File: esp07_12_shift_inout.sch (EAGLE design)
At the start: 47 parts, among them IC1 74HCT595D, IC2 74HCT595D, IC3 74HC165D, IC4 74HC165D

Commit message: Another approximation
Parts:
- JP11, JP12: value M02PTH3 -> (none); device SparkFun-Connectors:M02PTH3 -> SparkFun-Connectors:M02PTH
- JP7: value M02PTH3 -> (none)
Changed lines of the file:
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@@
 <part name="P+15" library="supply1" deviceset="VCC" device=""/>
 <part name="GND18" library="supply1" deviceset="GND" device=""/>
-<part name="JP11" library="SparkFun-Connectors" deviceset="M02" device="PTH3"/>
-<part name="JP12" library="SparkFun-Connectors" deviceset="M02" device="PTH3"/>
+<part name="JP11" library="SparkFun-Connectors" deviceset="M02" device="PTH"/>
+<part name="JP12" library="SparkFun-Connectors" deviceset="M02" device="PTH"/>
 <part name="GND19" library="supply1" deviceset="GND" device=""/>
 <part name="GND20" library="supply1" deviceset="GND" device=""/>

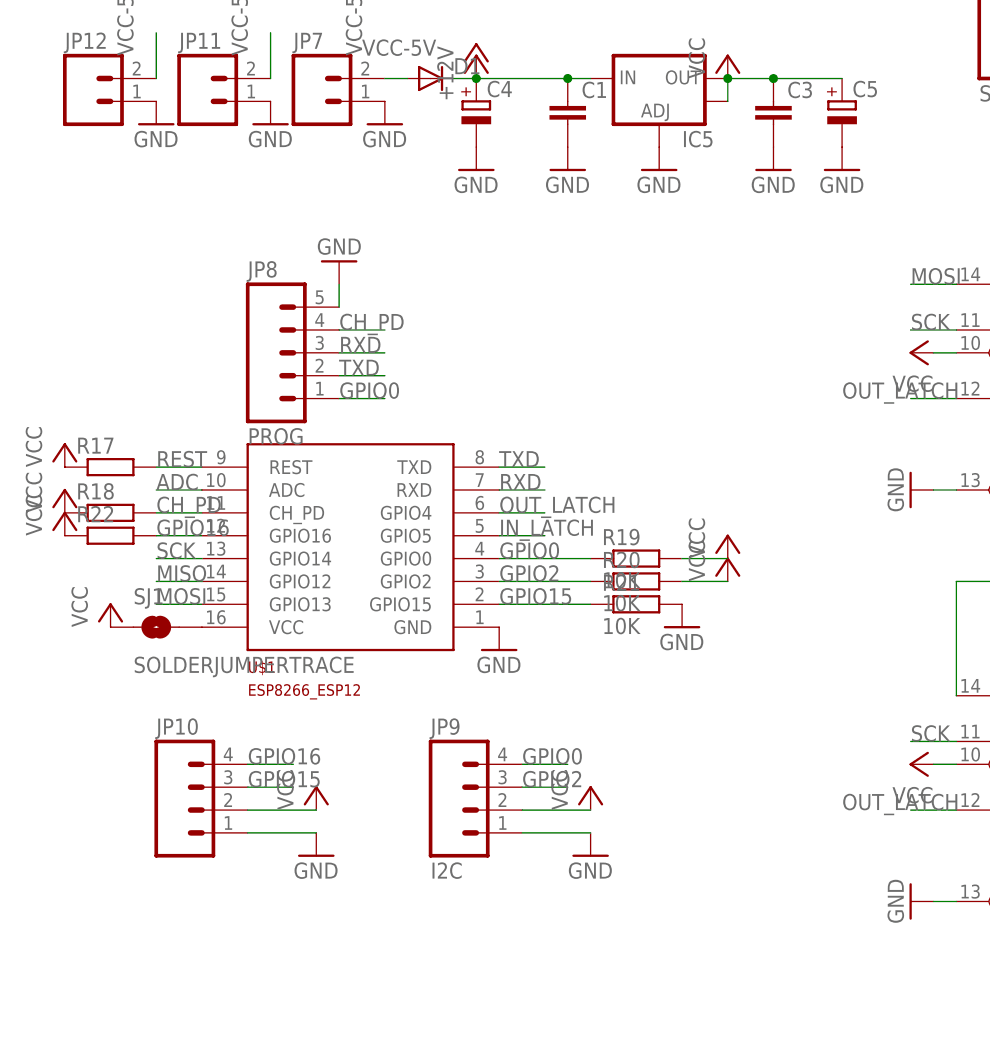
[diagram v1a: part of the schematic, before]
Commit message: * Change ESP module to ESP-12E footprint. Change ESP resistors to 0603. Change *_LATCH pins to 15,16
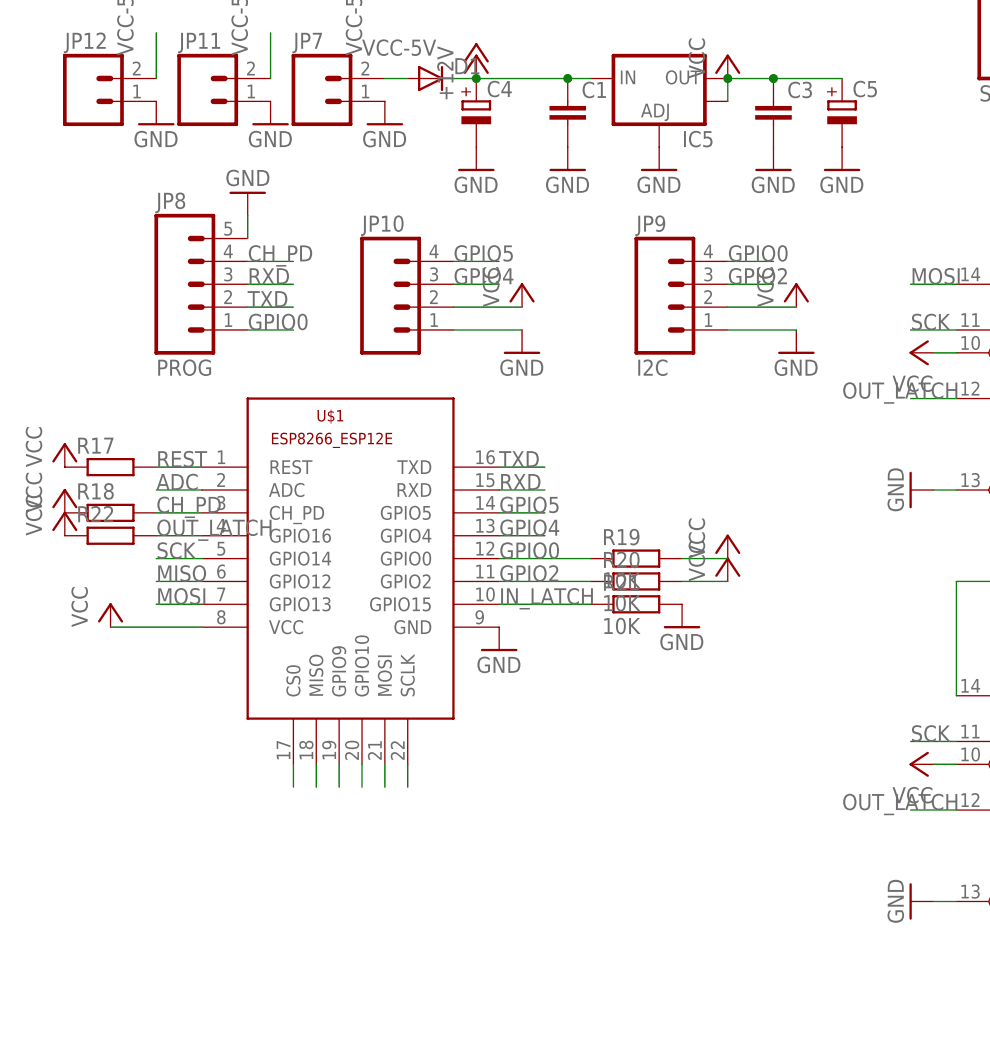
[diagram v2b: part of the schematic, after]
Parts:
- removed SJ1: SOLDERJUMPERTRACE, SparkFun-Retired:SOLDERJUMPERTRACE
- R17, R18, R19, R20, R21, R22: device rcl:R-EU_M0805 -> rcl:R-EU_R0603
- U$1: value ESP8266_ESP-12 -> (none); device esp8266_esp12:ESP8266_ESP-12 -> ESP8266-ESP12E:ESP8266-12EESP8266-ESP12E
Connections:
- removed net GPIO15: JP10.3, R21.1, U$1.GPIO15
- removed net GPIO16: JP10.4, R22.2, U$1.GPIO16
- removed net N$36: SJ1.2, U$1.VCC
- new net GPIO4: JP10.3, U$1.GPIO4
- new net GPIO5: JP10.4, U$1.GPIO5
- new net N$35: U$1.CS0
- new net N$37: U$1.MISO
- new net N$38: U$1.GPIO9
- new net N$39: U$1.GPIO10
- new net N$40: U$1.MOSI
- new net N$41: U$1.SCLK
- net IN_LATCH: now also R21.1, U$1.GPIO15; no longer U$1.GPIO5
- net OUT_LATCH: now also R22.2, U$1.GPIO16; no longer U$1.GPIO4
- net VCC: now also U$1.VCC; no longer SJ1.1
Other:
- moved on the sheet: JP10, JP8, JP9

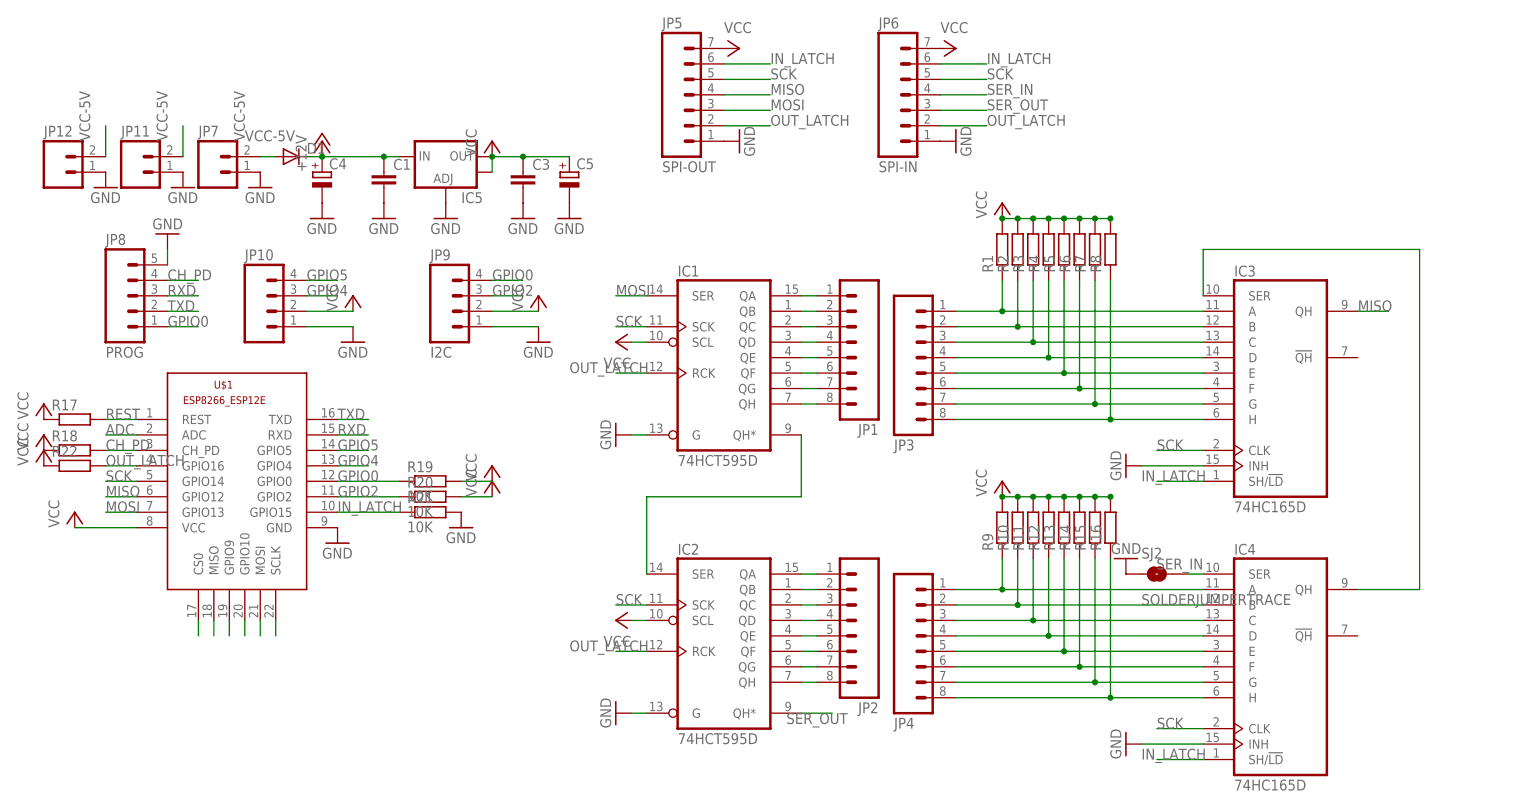
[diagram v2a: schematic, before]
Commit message: * Change OUT connectors to 2x10 and add GND / VCC pins to them
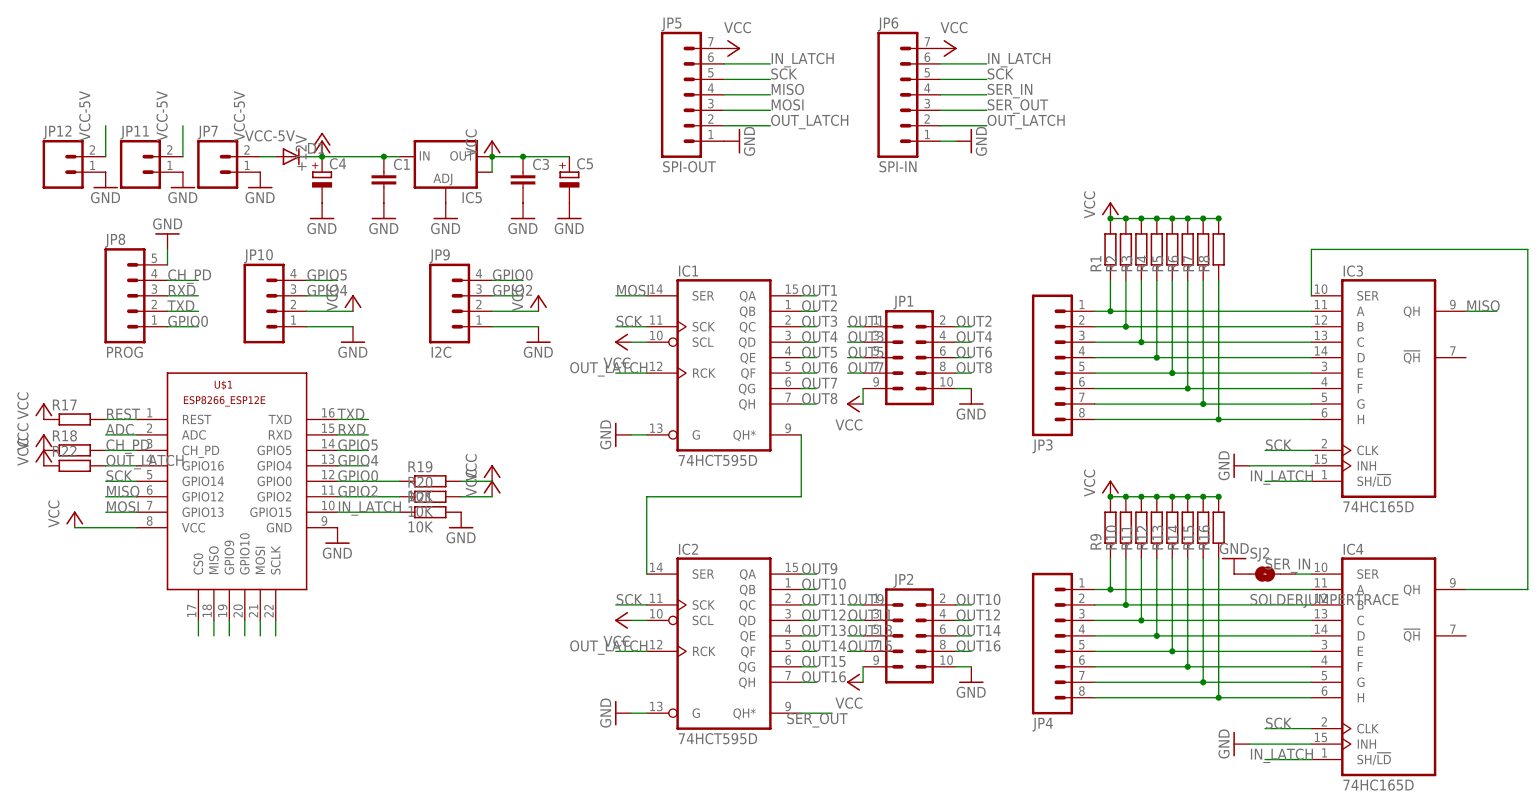
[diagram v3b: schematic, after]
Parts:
- JP1, JP2: device SparkFun-Connectors:M08SILK_FEMALE_PTH -> SparkFun-Connectors:M05X2PTH
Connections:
- net N$10 renamed OUT8
- net N$11 renamed OUT9
- net N$12 renamed OUT10
- net N$13 renamed OUT11
- net N$14 renamed OUT12
- net N$15 renamed OUT13
- net N$16 renamed OUT14
- net N$17 renamed OUT15
- net N$18 renamed OUT16
- net N$3 renamed OUT1
- net N$4 renamed OUT2
- net N$5 renamed OUT3
- net N$6 renamed OUT4
- net N$7 renamed OUT5
- net N$8 renamed OUT6
- net N$9 renamed OUT7
- net GND: now also JP1.10, JP2.10
- net VCC: now also JP1.9, JP2.9
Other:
- moved on the sheet: IC3, IC4, JP3, JP4, R1, R10, R11, R12, R13, R14, R15, R16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

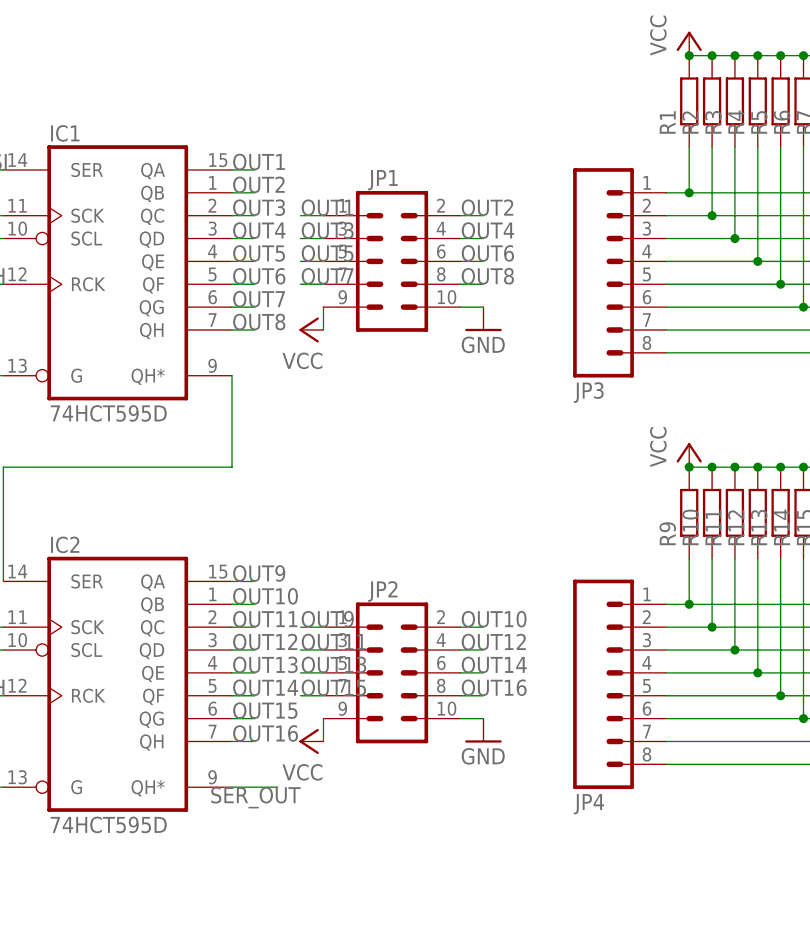
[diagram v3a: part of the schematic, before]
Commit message: * Change OUT pins configuration to pin 1 - GND, pin 10 - VCC
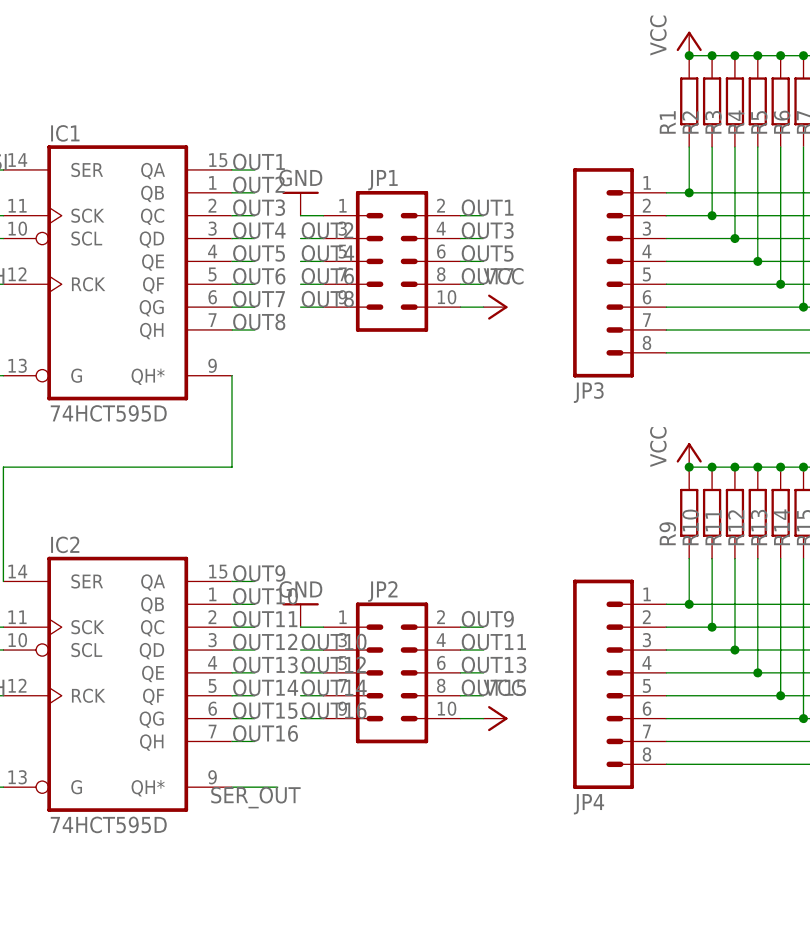
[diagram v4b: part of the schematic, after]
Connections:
- net GND: now also JP1.1, JP2.1; no longer JP1.10, JP2.10
- net OUT1: now also JP1.2; no longer JP1.1
- net OUT10: now also JP2.3; no longer JP2.2
- net OUT11: now also JP2.4; no longer JP2.3
- net OUT12: now also JP2.5; no longer JP2.4
- net OUT13: now also JP2.6; no longer JP2.5
- net OUT14: now also JP2.7; no longer JP2.6
- net OUT15: now also JP2.8; no longer JP2.7
- net OUT16: now also JP2.9; no longer JP2.8
- net OUT2: now also JP1.3; no longer JP1.2
- net OUT3: now also JP1.4; no longer JP1.3
- net OUT4: now also JP1.5; no longer JP1.4
- net OUT5: now also JP1.6; no longer JP1.5
- net OUT6: now also JP1.7; no longer JP1.6
- net OUT7: now also JP1.8; no longer JP1.7
- net OUT8: now also JP1.9; no longer JP1.8
- net OUT9: now also JP2.2; no longer JP2.1
- net VCC: now also JP1.10, JP2.10; no longer JP1.9, JP2.9

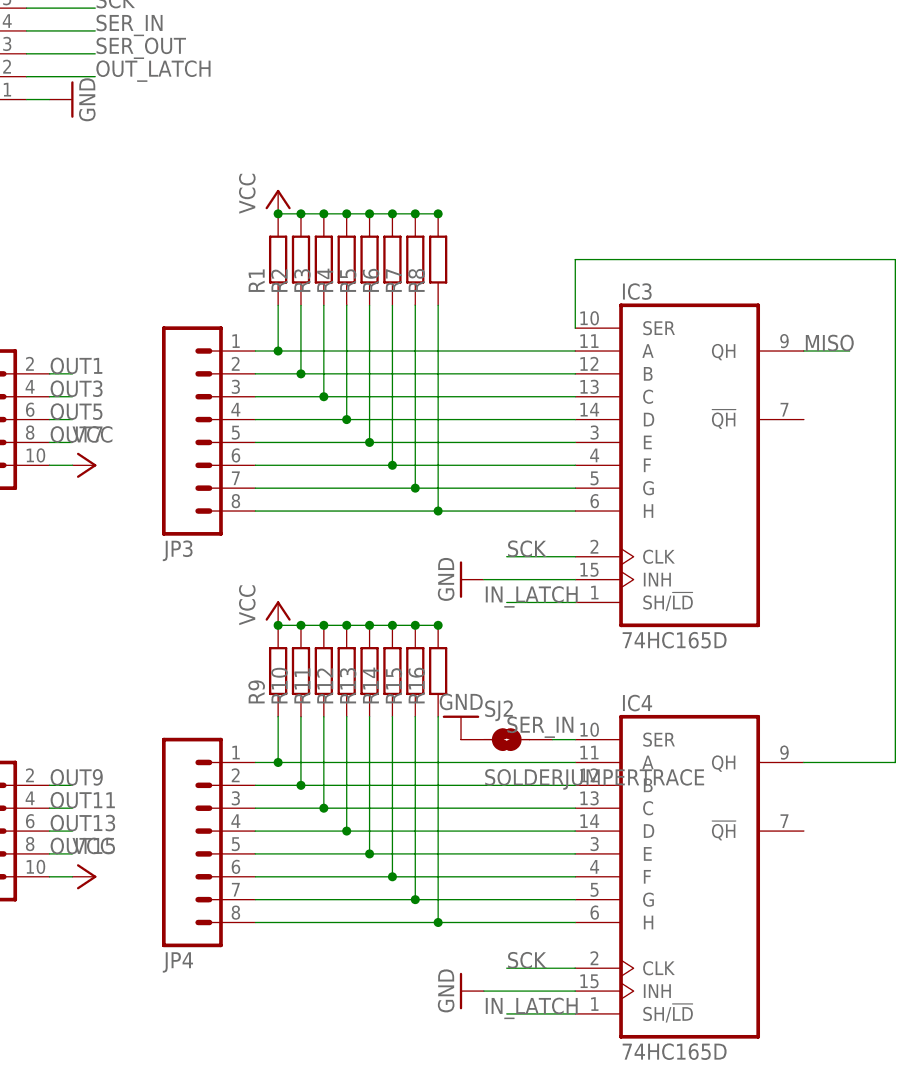
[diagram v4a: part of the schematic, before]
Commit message: * Finish new version of PCB.
* Change ESP module to ESP-12E with additional (but useless) pins
* Change OUT_ IN_ latch to 15,16
* Change OUT_ IN_ connection to 2x5 header
* Remove pull-up resistors on IN_ part in favour to implement them in add-on opto-isolated IN PCB
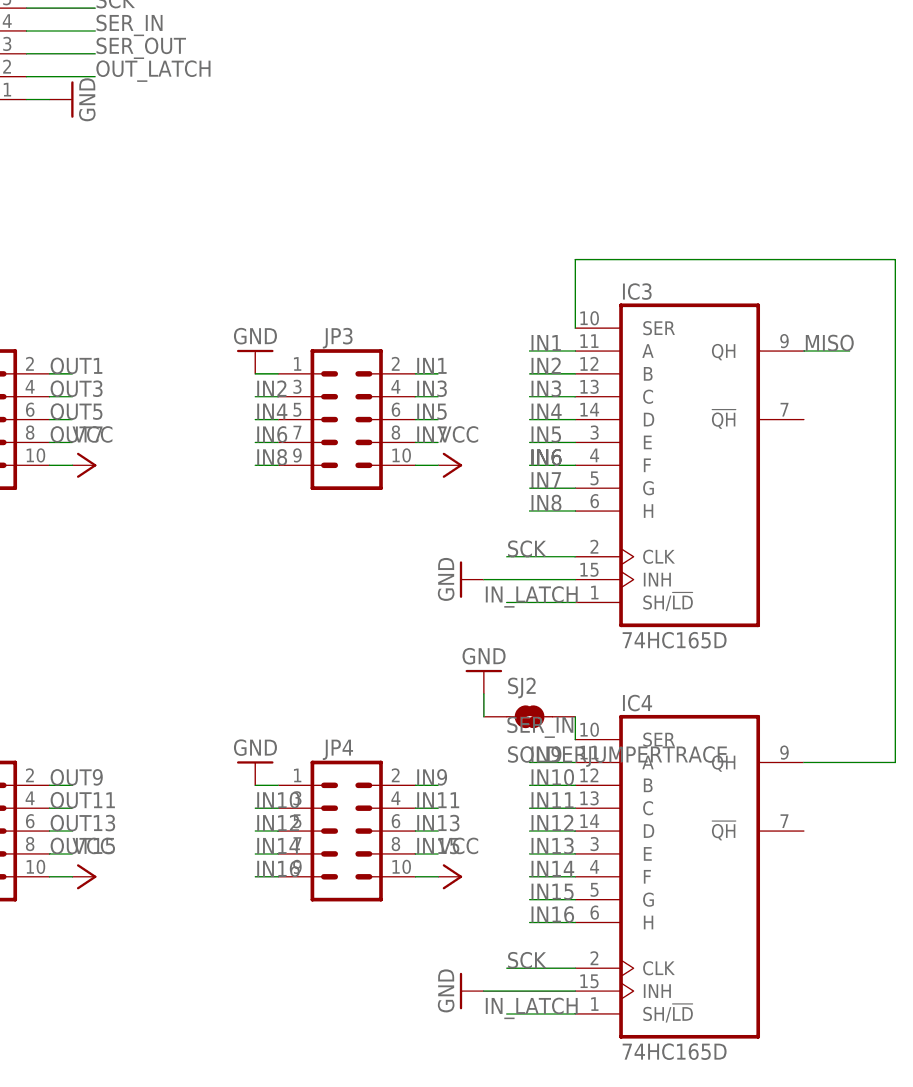
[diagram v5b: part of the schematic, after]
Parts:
- removed R1, R10, R11, R12, R13, R14, R15, R16, R2, R3, R4, R5, R6, R7, R8, R9: (no value), rcl:R-EU_M0805
- JP1, JP2: device SparkFun-Connectors:M05X2PTH -> SparkFun-Connectors:M05X2SHD
- JP3, JP4: device SparkFun-Connectors:M08SILK_FEMALE_PTH -> SparkFun-Connectors:M05X2SHD
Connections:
- removed net N$19: IC3A.A, JP3.1, R1.1
- removed net N$20: IC3A.B, JP3.2, R2.1
- removed net N$21: IC3A.C, JP3.3, R3.1
- removed net N$22: IC3A.D, JP3.4, R4.1
- removed net N$23: IC3A.E, JP3.5, R5.1
- removed net N$24: IC3A.F, JP3.6, R6.1
- removed net N$25: IC3A.G, JP3.7, R7.1
- removed net N$26: IC3A.H, JP3.8, R8.1
- removed net N$27: IC4A.A, JP4.1, R9.1
- removed net N$28: IC4A.B, JP4.2, R10.1
- removed net N$29: IC4A.C, JP4.3, R11.1
- removed net N$30: IC4A.D, JP4.4, R12.1
- removed net N$31: IC4A.E, JP4.5, R13.1
- removed net N$32: IC4A.F, JP4.6, R14.1
- removed net N$33: IC4A.G, JP4.7, R15.1
- removed net N$34: IC4A.H, JP4.8, R16.1
- new net IN1: IC3A.A, JP3.2
- new net IN10: IC4A.B, JP4.3
- new net IN11: IC4A.C, JP4.4
- new net IN12: IC4A.D, JP4.5
- new net IN13: IC4A.E, JP4.6
- new net IN14: IC4A.F, JP4.7
- new net IN15: IC4A.G, JP4.8
- new net IN16: IC4A.H, JP4.9
- new net IN2: IC3A.B, JP3.3
- new net IN3: IC3A.C, JP3.4
- new net IN4: IC3A.D, JP3.5
- new net IN5: IC3A.E, JP3.6
- new net IN6: IC3A.F, JP3.7
- new net IN7: IC3A.G, JP3.8
- new net IN8: IC3A.H, JP3.9
- new net IN9: IC4A.A, JP4.2
- net GND: now also JP3.1, JP4.1
- net VCC: now also JP3.10, JP4.10; no longer R1.2, R10.2, R11.2, R12.2, R13.2, R14.2, R15.2, R16.2, R2.2, R3.2, R4.2, R5.2, R6.2, R7.2, R8.2, R9.2
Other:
- moved on the sheet: SJ2
